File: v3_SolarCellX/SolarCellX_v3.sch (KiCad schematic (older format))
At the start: 13 parts, among them IC1 symbols_TSL2561, J1 symbols_XF2M-1015-1A

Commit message: Cleaned up the Magnetorquer and added labels
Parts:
- removed IC1: symbols_TSL2561, TSL2561, symbol misc-circuits-cache:symbols_TSL2561
- removed J1: symbols_XF2M-1015-1A, XF2M-1015-1A, symbol misc-circuits-cache:symbols_XF2M-1015-1A
- added C5: 0.1uF, Capacitor_SMD:C_0402_1005Metric, symbol SolarCellX_v3-rescue:0.1UF-0603-25V-(+80_-20%)-misc-circuits-cache-misc-circuit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
- added IC1: TSL2561, misc-circuits:TSL2561, symbol SolarCellX_v3-rescue:TSL2561-symbols-misc-circuits-rescue
- added J1: XF2M-1015-1A, misc-circuits:XF2M-1015-1A, symbol SolarCellX_v3-rescue:XF2M-1015-1A-symbols-misc-circuits-rescue
- added R12, R13: 0, Resistor_SMD:R_0402_1005Metric, symbol SolarCellX_v3-rescue:0OHM-0603-1_10W-5%-misc-circuits-cache-misc-circuits-rescue
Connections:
- net labels added: +3V3, BATT_N, BATT_P, BURN1, COIL_N, COIL_P, GND, SCL1, SDA1, VSolar
- wire segments 30 -> 52
- no-connect marks 0 -> 1

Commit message: making libraries locally referenced for easy import
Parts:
- removed C5: 0.1uF, Capacitor_SMD:C_0402_1005Metric, symbol SolarCellX_v3-rescue:0.1UF-0603-25V-(+80_-20%)-misc-circuits-cache-misc-circuit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
- removed IC1: TSL2561, misc-circuits:TSL2561, symbol SolarCellX_v3-rescue:TSL2561-symbols-misc-circuits-rescue
- removed R12, R13: 0, Resistor_SMD:R_0402_1005Metric, symbol SolarCellX_v3-rescue:0OHM-0603-1_10W-5%-misc-circuits-cache-misc-circuits-rescue
- added C1, C10, C13, C3, C9: 0.1uF, Capacitor_SMD:C_0402_1005Metric, symbol misc-circuits-rescue:0.1UF-0603-25V-(+80_-20%)-misc-circuits-cache
- added C11, C12, C14, C6: 100uF, Capacitor_SMD:C_0603_1608Metric, symbol misc-circuits-rescue:0.1UF-0603-25V-(+80_-20%)-misc-circuits-cache
- added C2: 1.0uF, Capacitor_SMD:C_0402_1005Metric, symbol misc-circuits-rescue:1.0UF-0603-16V-10%-misc-circuits-cache
- added C4, C8: 4.7uF, Capacitor_SMD:C_0402_1005Metric, symbol misc-circuits-rescue:4.7UF0603-misc-circuits-cache
- added C5: 10nF, Capacitor_SMD:C_0402_1005Metric, symbol misc-circuits-rescue:10NF-0603-50V-10%-misc-circuits-cache
- added C7: 22uF, Capacitor_SMD:C_0402_1005Metric, symbol misc-circuits-rescue:22UF-0805-6.3V-20%-misc-circuits-cache
- added D4: SDM20U40-7, misc-circuits:SOD523, symbol misc-circuits-rescue:DIODE-SOD523-misc-circuits-cache
- added D5: MSS1P4-M3_89A, custom-footprints:MICROSMP, symbol symbols:MSS1P4-M3_89A
- added L1: 22uH-LPS4018-223MR, misc-circuits:LPS4018, symbol misc-circuits-rescue:COILCRAFT-LPS4018-misc-circuits-cache
- added L2: 10uH-LPS4018-103MR, misc-circuits:LPS4018, symbol misc-circuits-rescue:COILCRAFT-LPS4018-misc-circuits-cache
- added R1, R11, R12, R13, R14, R15, R2, R3: 0, Resistor_SMD:R_0402_1005Metric, symbol misc-circuits-rescue:0OHM-0603-1_10W-5%-misc-circuits-cache
- added R10: 4.75M, Resistor_SMD:R_0402_1005Metric, symbol misc-circuits-rescue:1MOHM-0603-1_4W-5%-misc-circuits-cache
- added R4: 7.32M, Resistor_SMD:R_0402_1005Metric, symbol misc-circuits-rescue:1MOHM-0603-1_4W-5%-misc-circuits-cache
- added R5: 5.62M, Resistor_SMD:R_0402_1005Metric, symbol misc-circuits-rescue:1MOHM-0603-1_4W-5%-misc-circuits-cache
- added R6: 374K, Resistor_SMD:R_0402_1005Metric, symbol misc-circuits-rescue:1MOHM-0603-1_4W-5%-misc-circuits-cache
- added R7, R9: 8.25M, Resistor_SMD:R_0402_1005Metric, symbol misc-circuits-rescue:1MOHM-0603-1_4W-5%-misc-circuits-cache
- added R8: 4.53M, Resistor_SMD:R_0402_1005Metric, symbol misc-circuits-rescue:1MOHM-0603-1_4W-5%-misc-circuits-cache
- added U1: Value, misc-circuits:QFN50P350X350X100-21N-D, symbol misc-circuits-rescue:BQ25570RGRR-misc-circuits-cache
- added U2: TSL2561, misc-circuits:TSL2561, symbol symbols:TSL2561
- D1, D2, D3: symbol SolarCellParts:SBDiode -> SolarCellX_v3-rescue:SBDiode-SolarCellParts
- SC1, SC2, SC3, SC4, SC5, SC6, SC7, SC8: symbol SolarCellParts:SolarCell_Small -> SolarCellX_v3-rescue:SolarCell_Small-SolarCellParts
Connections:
- net labels added: VBAT, VBAT_OK, VOUT_EN, VSOLAR
- wire segments 52 -> 161
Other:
- note added: "80% MPPT"
- note added: "BQ25570RGRR"
- note added: "DNI"
- note added: "Energy Harvesting IC"
- note added: "External energy storage\nInput/Output"
- note added: "External\nPower Source\nInput\n(Solar)"
- note added: "Imin=280uA"
- note added: "MPPT Set Resistors"
- note added: "Sets of resistor dividers should = 13MOhm"
- note added: "VBAT_OK\nON: 3.51V\nOFF: 3.42V"
- note added: "VBAT_OV\n4.2V"
- note added: "VOUT=1.21V*((ROUT2+ROUT1)/ROUT1)"
- note added: "VOUT\n3.31"
- note added: "ZENER"

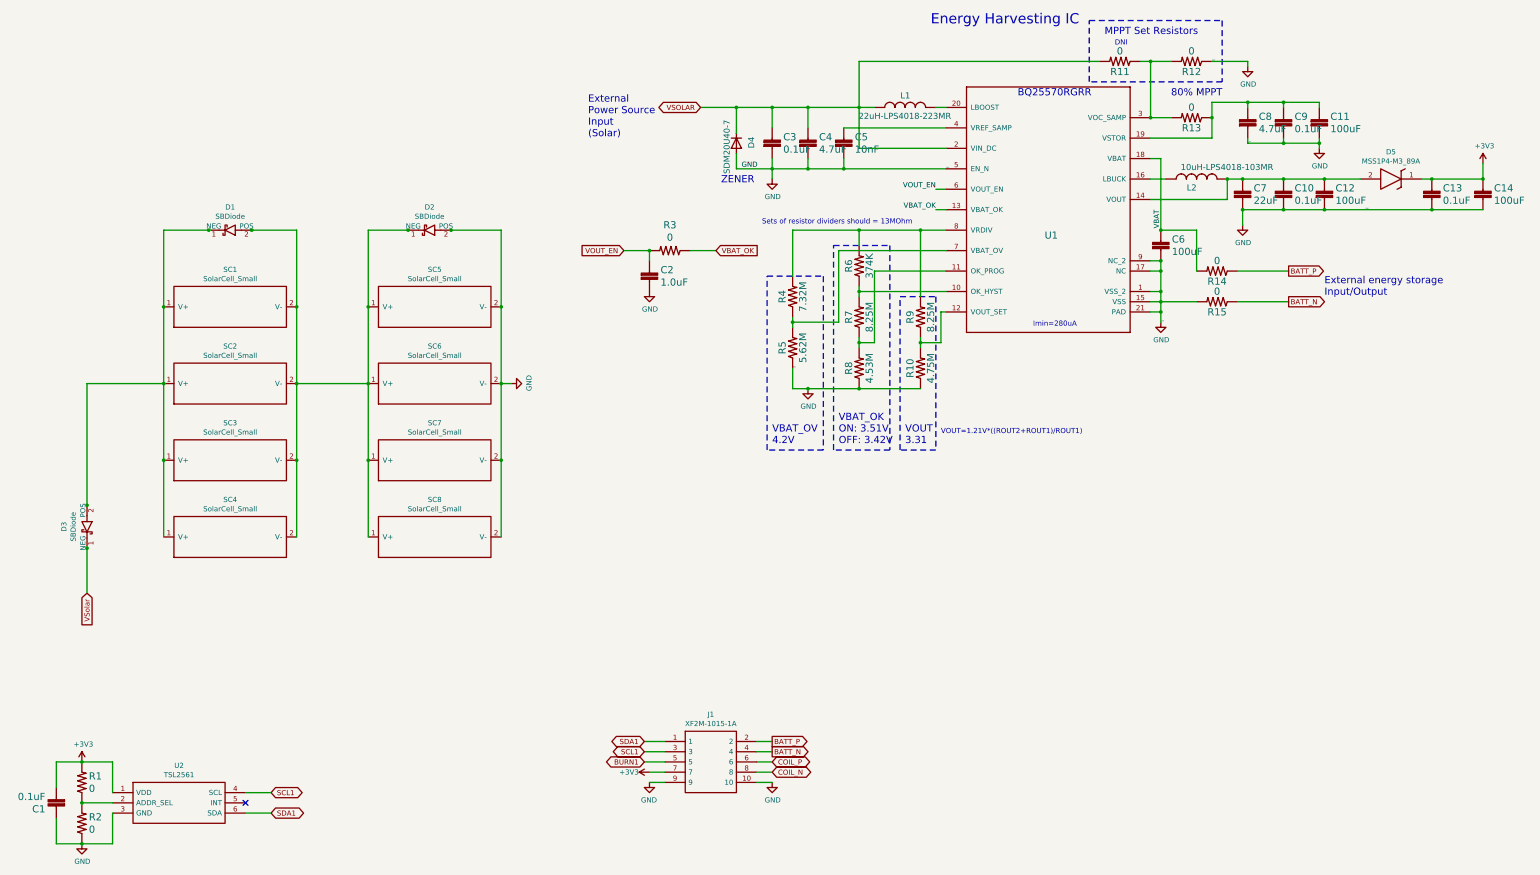
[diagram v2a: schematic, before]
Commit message: circuits added and coil connection made
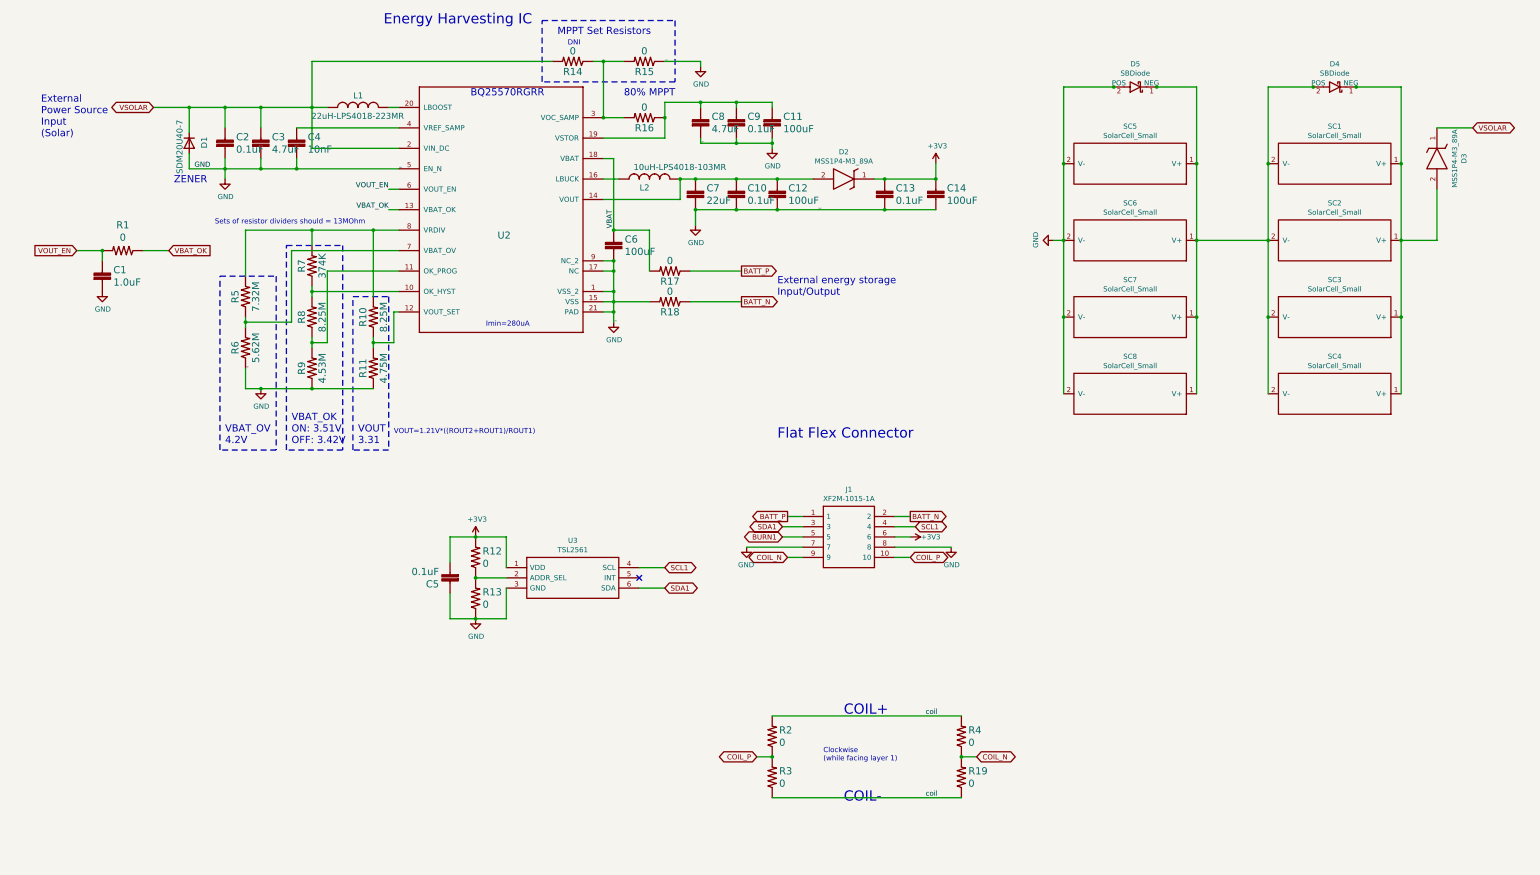
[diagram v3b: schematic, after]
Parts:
- removed C1, C10, C13, C3, C9: 0.1uF, Capacitor_SMD:C_0402_1005Metric, symbol misc-circuits-rescue:0.1UF-0603-25V-(+80_-20%)-misc-circuits-cache
- removed C11, C12, C14, C6: 100uF, Capacitor_SMD:C_0603_1608Metric, symbol misc-circuits-rescue:0.1UF-0603-25V-(+80_-20%)-misc-circuits-cache
- removed C2: 1.0uF, Capacitor_SMD:C_0402_1005Metric, symbol misc-circuits-rescue:1.0UF-0603-16V-10%-misc-circuits-cache
- removed C4, C8: 4.7uF, Capacitor_SMD:C_0402_1005Metric, symbol misc-circuits-rescue:4.7UF0603-misc-circuits-cache
- removed C5: 10nF, Capacitor_SMD:C_0402_1005Metric, symbol misc-circuits-rescue:10NF-0603-50V-10%-misc-circuits-cache
- removed C7: 22uF, Capacitor_SMD:C_0402_1005Metric, symbol misc-circuits-rescue:22UF-0805-6.3V-20%-misc-circuits-cache
- removed D3: SBDiode, SolarCellParts:SB Diode, symbol SolarCellX_v3-rescue:SBDiode-SolarCellParts
- removed D4: SDM20U40-7, misc-circuits:SOD523, symbol misc-circuits-rescue:DIODE-SOD523-misc-circuits-cache
- removed D5: MSS1P4-M3_89A, custom-footprints:MICROSMP, symbol symbols:MSS1P4-M3_89A
- removed J1: XF2M-1015-1A, misc-circuits:XF2M-1015-1A, symbol SolarCellX_v3-rescue:XF2M-1015-1A-symbols-misc-circuits-rescue
- removed L1: 22uH-LPS4018-223MR, misc-circuits:LPS4018, symbol misc-circuits-rescue:COILCRAFT-LPS4018-misc-circuits-cache
- removed L2: 10uH-LPS4018-103MR, misc-circuits:LPS4018, symbol misc-circuits-rescue:COILCRAFT-LPS4018-misc-circuits-cache
- removed R1, R11, R12, R13, R14, R15, R2, R3: 0, Resistor_SMD:R_0402_1005Metric, symbol misc-circuits-rescue:0OHM-0603-1_10W-5%-misc-circuits-cache
- removed R10: 4.75M, Resistor_SMD:R_0402_1005Metric, symbol misc-circuits-rescue:1MOHM-0603-1_4W-5%-misc-circuits-cache
- removed R4: 7.32M, Resistor_SMD:R_0402_1005Metric, symbol misc-circuits-rescue:1MOHM-0603-1_4W-5%-misc-circuits-cache
- removed R5: 5.62M, Resistor_SMD:R_0402_1005Metric, symbol misc-circuits-rescue:1MOHM-0603-1_4W-5%-misc-circuits-cache
- removed R6: 374K, Resistor_SMD:R_0402_1005Metric, symbol misc-circuits-rescue:1MOHM-0603-1_4W-5%-misc-circuits-cache
- removed R7, R9: 8.25M, Resistor_SMD:R_0402_1005Metric, symbol misc-circuits-rescue:1MOHM-0603-1_4W-5%-misc-circuits-cache
- removed R8: 4.53M, Resistor_SMD:R_0402_1005Metric, symbol misc-circuits-rescue:1MOHM-0603-1_4W-5%-misc-circuits-cache
- removed U1: Value, misc-circuits:QFN50P350X350X100-21N-D, symbol misc-circuits-rescue:BQ25570RGRR-misc-circuits-cache
- removed U2: TSL2561, misc-circuits:TSL2561, symbol symbols:TSL2561
- added C1: 1.0uF, Capacitor_SMD:C_0402_1005Metric, symbol SolarCellX_v3-rescue:1.0UF-0603-16V-10%-misc-circuits-cache-misc-circuits-rescue
- added C10, C13, C2, C5: 0.1uF, Capacitor_SMD:C_0402_1005Metric, symbol SolarCellX_v3-rescue:0.1UF-0603-25V-(+80_-20%)-misc-circuits-cache-misc-circuit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
- added C11, C12: 100uF, Capacitor_SMD:C_0603_1608Metric, symbol SolarCellX_v3-rescue:0.1UF-0603-25V-(+80_-20%)-misc-circuits-cache-misc-circuit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
- added C14, C6: 100uF, Capacitor_SMD:C_0402_1005Metric, symbol SolarCellX_v3-rescue:0.1UF-0603-25V-(+80_-20%)-misc-circuits-cache-misc-circuit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
- added C3, C8: 4.7uF, Capacitor_SMD:C_0402_1005Metric, symbol SolarCellX_v3-rescue:4.7UF0603-misc-circuits-cache-misc-circuits-rescue
- added C4: 10nF, Capacitor_SMD:C_0402_1005Metric, symbol SolarCellX_v3-rescue:10NF-0603-50V-10%-misc-circuits-cache-misc-circuits-rescue
- added C7: 22uF, Capacitor_SMD:C_0402_1005Metric, symbol SolarCellX_v3-rescue:22UF-0805-6.3V-20%-misc-circuits-cache-misc-circuits-rescue
- added C9: 0.1uF, Capacitor_SMD:C_0603_1608Metric, symbol SolarCellX_v3-rescue:0.1UF-0603-25V-(+80_-20%)-misc-circuits-cache-misc-circuit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
- added D1: SDM20U40-7, custom-footprints:MICROSMP, symbol SolarCellX_v3-rescue:DIODE-SOD523-misc-circuits-cache-misc-circuits-rescue
- added D2, D3: MSS1P4-M3_89A, custom-footprints:MICROSMP, symbol symbols:MSS1P4-M3_89A
- added J1: XF2M-1015-1A, custom-footprints:XF2M-1015-1A, symbol symbols:XF2M-1015-1A
- added L1: 22uH-LPS4018-223MR, misc-circuits:LPS4018, symbol SolarCellX_v3-rescue:COILCRAFT-LPS4018-misc-circuits-cache-misc-circuits-rescue
- added L2: 10uH-LPS4018-103MR, misc-circuits:LPS4018, symbol SolarCellX_v3-rescue:COILCRAFT-LPS4018-misc-circuits-cache-misc-circuits-rescue
- added R1, R12, R13, R14, R15, R16, R17, R18, R19, R2, R3, R4: 0, Resistor_SMD:R_0402_1005Metric, symbol SolarCellX_v3-rescue:0OHM-0603-1_10W-5%-misc-circuits-cache-misc-circuits-rescue
- added R10, R8: 8.25M, Resistor_SMD:R_0402_1005Metric, symbol SolarCellX_v3-rescue:1MOHM-0603-1_4W-5%-misc-circuits-cache-misc-circuits-rescue
- added R11: 4.75M, Resistor_SMD:R_0402_1005Metric, symbol SolarCellX_v3-rescue:1MOHM-0603-1_4W-5%-misc-circuits-cache-misc-circuits-rescue
- added R5: 7.32M, Resistor_SMD:R_0402_1005Metric, symbol SolarCellX_v3-rescue:1MOHM-0603-1_4W-5%-misc-circuits-cache-misc-circuits-rescue
- added R6: 5.62M, Resistor_SMD:R_0402_1005Metric, symbol SolarCellX_v3-rescue:1MOHM-0603-1_4W-5%-misc-circuits-cache-misc-circuits-rescue
- added R7: 374K, Resistor_SMD:R_0402_1005Metric, symbol SolarCellX_v3-rescue:1MOHM-0603-1_4W-5%-misc-circuits-cache-misc-circuits-rescue
- added R9: 4.53M, Resistor_SMD:R_0402_1005Metric, symbol SolarCellX_v3-rescue:1MOHM-0603-1_4W-5%-misc-circuits-cache-misc-circuits-rescue
- added U2: Value, custom-footprints:NDS8434, symbol SolarCellX_v3-rescue:BQ25570RGRR-misc-circuits-cache-misc-circuits-rescue
- added U3: TSL2561, misc-circuits:TSL2561, symbol symbols:TSL2561
- renumbered D1 to D4, D2 to D5
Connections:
- net labels added: coil
- net labels removed: VSolar
- wire segments 161 -> 163
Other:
- note added: "COIL+"
- note added: "COIL-"
- note added: "Clockwise\n(while facing layer 1)"
- note added: "Flat Flex Connector"
- moved on the sheet: D4, D5, SC1, SC2, SC3, SC4, SC5, SC6, SC7, SC8
